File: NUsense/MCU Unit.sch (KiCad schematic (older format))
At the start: 40 parts

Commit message: Correct broken files
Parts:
- removed C? (x13): C, symbol C
- removed R? (x3): R, symbol R
- added C? (x2): 4.7uF, symbol CP
- added C?: 1uF, symbol CP
- added C? (x19): 100nF, symbol C
- added C?: 9pF, symbol C
- added C?: 8pF, symbol C
- added R? (x3): 0, symbol R
- C?: value C -> 9pF
- C?: value C -> 8pF
- C? (x3): value C -> 1uF
- C? (x2): value C -> 0.1uF
- C? (x2): value C -> 2.2uF
- C?: value C -> 100nF
- R? (x2): value R -> 0
- R? (x2): value R -> 10K
- R?: value R -> NC
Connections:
- net labels added: +3.3V, BUZZER_SIG, JTCK_SWCLK, JTD0_SW0, JTDI, JTMS_SWDIO, MCU_RESET, MPU_INT, MPU_SCL, MPU_SDA/SDI, OTG_HS_ULPI_CK, OTG_HS_ULPI_D, OTG_HS_ULPI_DIR, OTG_HS_ULPI_NXT, OTG_HS_ULPI_STP, UART5_RX, UART5_TX, UART7_RX, UART7_TX, UART8_RX, UART8_TX, USART1_RX, USART1_TX, USART2_RX, USART2_TX, USART3_RX, USART3_TX, USART6_RX, USART6_TX
- net labels removed: MCU_NRESET, VDD3o3V
- wire segments 95 -> 145
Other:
- moved on the sheet: C?

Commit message: Main page additions
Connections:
- net labels added: I2C4_INT, I2C4_SCL, I2C4_SDA
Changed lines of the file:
@@
 Text HLabel 12300 7100 0    60   Output ~ 0
 BUZZER_SIG
+Text HLabel 12300 3600 0    60   BiDi ~ 0
+I2C4_SDA
+Text HLabel 12300 3500 0    60   BiDi ~ 0
+I2C4_SCL
+Text HLabel 12300 3400 0    60   BiDi ~ 0
+I2C4_INT
 $EndSCHEMATC

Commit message: Footprints
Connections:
- net labels added: VS_ALERT
- net labels removed: I2C4_INT
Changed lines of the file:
@@
 I2C4_SCL
 Text HLabel 12300 3400 0    60   BiDi ~ 0
-I2C4_INT
+VS_ALERT
 $EndSCHEMATC

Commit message: Adds annotations and footprints
Changes crystal selection
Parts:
- removed C?: 9pF, symbol C
- removed R? (x4): 0, symbol R
- removed Y?: STL9020C-32.768K, symbol STL9020C-32.768K
- removed Y?: SP8150E7-25.000M, symbol SP8150E7-25.000M
- added C310: 10pF, Capacitors_SMD:C_0805_HandSoldering, symbol C
- added X1: 24MHz, Footprints:XTAL-OSC, symbol Crystal_GND24
- added X2: ST3215SB32768H5, Footprints:XTAL, symbol Crystal
- C301, C302, C303, C304, C305, C306, C307, C308, C311, C312, C313, C314, C315, C316, C317, C318, C319, C320, C321, C322, C323, C324, C325, C326, C327, C328, C329, C330, C331, C332, C333, C334: renamed from C?; footprint (none) -> Capacitors_SMD:C_0805_HandSoldering
- C309: renamed from C?; value 9pF -> 10pF; footprint (none) -> Capacitors_SMD:C_0805_HandSoldering
- R305, R306, R307, R308: renamed from R?; footprint (none) -> Resistors_SMD:R_0805_HandSoldering
- U301: renamed from U?; footprint (none) -> Footprints:LQFP144
- gave numbers to parts that had none: 4
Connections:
- net labels added: OSC32_IN, OSC32_OUT, OSC_IN, OSC_OUT, UART5_EN, USART1_EN, USART2_EN, USART3_EN, USART6_EN
- net labels removed: UART7_RX, UART7_TX, UART8_RX, UART8_TX
- wire segments 145 -> 141
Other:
- moved on the sheet: C309, C311, C312

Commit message: More Changes
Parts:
- renumbered C311 to C309, C309 to C310, C313 to C311, C314 to C312, C315 to C313, C316 to C314, C317 to C315, C318 to C316, C312 to C317, C319 to C318, C320 to C319, C310 to C320, R305 to R301, R306 to R302, R307 to R303, R308 to R304, X1 to X301, X2 to X302
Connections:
- net DXL_PWR_EN: now reaches U301.55 (PF15)

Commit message: Buttons/LEDs
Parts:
- added H?: LED_HEADER, symbol LED_HEADER
- added H?: BUT_HEADER, symbol BUT_HEADER
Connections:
- net +3V3: now also H?.3
- net GND: now also H?.1
- new net LED2: H?.7
- new net LED3: H?.6
- new net LED4: H?.5
- new net LED5_B: H?.2
- new net LED5_G: H?.3
- new net LED5_R: H?.4
- new net LED6_B: H?.7
- new net LED6_G: H?.8
- new net LED6_R: H?.1
- new net LED_RX: H?.8
- new net LED_TX: H?.9
- new net RESET: H?.6
- new net SW_MODE: H?.5
- new net SW_START: H?.4
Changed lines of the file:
@@
 Text HLabel 12300 7200 0    60   Output ~ 0
 DXL_PWR_EN
+$Comp
+L LED_HEADER H?
+U 1 1 5A74166C
+P 14650 9700
+F 0 "H?" H 14750 10850 60  0000 C CNN
+F 1 "LED_HEADER" H 14750 9650 60  0000 C CNN
+F 2 "" H 14650 9700 60  0001 C CNN
+F 3 "" H 14650 9700 60  0001 C CNN
+	1    14650 9700
+	1    0    0    -1
+$EndComp
+Wire Wire Line
+	14450 7450 14350 7450
+Wire Wire Line
+	14350 7450 14350 7150
+Wire Wire Line
+	14350 7150 15050 7150
+Wire Wire Line
+	15050 7150 15050 7350
+Wire Wire Line
+	14450 7550 14100 7550
+Wire Wire Line
+	13850 7650 14450 7650
+Wire Wire Line
+	14450 7750 14100 7750
+Wire Wire Line
+	14450 7850 14100 7850
+Wire Wire Line
+	14450 7950 14100 7950
+Wire Wire Line
+	14450 8050 14100 8050
+Wire Wire Line
+	14450 8150 14100 8150
+Text Label 14100 8150 0    60   ~ 0
+LED6_G
+Text Label 14100 8050 0    60   ~ 0
+LED6_B
+Text Label 14100 7950 0    60   ~ 0
+RESET
+Text Label 14100 7850 0    60   ~ 0
+SW_MODE
+Text Label 14100 7750 0    60   ~ 0
+SW_START
+$Comp
+L +3.3V #PWR?
+U 1 1 5A742C85
+P 13850 7600
+F 0 "#PWR?" H 13850 7450 50  0001 C CNN
+F 1 "+3.3V" H 13850 7740 50  0000 C CNN
+F 2 "" H 13850 7600 50  0001 C CNN
+F 3 "" H 13850 7600 50  0001 C CNN
+	1    13850 7600
+	1    0    0    -1
+$EndComp
+Wire Wire Line
+	13850 7600 13850 7650
+$Comp
+L BUT_HEADER H?
+U 1 1 5A743338
+P 14650 8450
+F 0 "H?" H 14750 9600 60  0000 C CNN
+F 1 "BUT_HEADER" H 14750 8600 60  0000 C CNN
+F 2 "" H 14650 8450 60  0001 C CNN
+F 3 "" H 14650 8450 60  0001 C CNN
+	1    14650 8450
+	1    0    0    -1
+$EndComp
+$Comp
+L GND #PWR?
+U 1 1 5A743470
+P 15050 7350
+F 0 "#PWR?" H 15050 7100 50  0001 C CNN
+F 1 "GND" H 15050 7200 50  0000 C CNN
+F 2 "" H 15050 7350 50  0001 C CNN
+F 3 "" H 15050 7350 50  0001 C CNN
+	1    15050 7350
+	1    0    0    -1
+$EndComp
+Wire Wire Line
+	14450 8700 14100 8700
+Wire Wire Line
+	14450 8800 14100 8800
+Wire Wire Line
+	14450 8900 14100 8900
+Wire Wire Line
+	14450 9000 14100 9000
+Wire Wire Line
+	14450 9100 14100 9100
+Wire Wire Line
+	14450 9200 14100 9200
+Wire Wire Line
+	14450 9300 14100 9300
+Wire Wire Line
+	14450 9400 14100 9400
+Wire Wire Line
+	14450 9500 14100 9500
+Text Label 14100 8700 0    60   ~ 0
+LED6_R
+Text Label 14100 8800 0    60   ~ 0
+LED5_B
+Text Label 14100 8900 0    60   ~ 0
+LED5_G
+Text Label 14100 9000 0    60   ~ 0
+LED5_R
+Text Label 14100 9100 0    60   ~ 0
+LED4
+Text Label 14100 9200 0    60   ~ 0
+LED3
+Text Label 14100 9300 0    60   ~ 0
+LED2
+Text Label 14100 9400 0    60   ~ 0
+LED_RX
+Text Label 14100 9500 0    60   ~ 0
+LED_TX
 $EndSCHEMATC

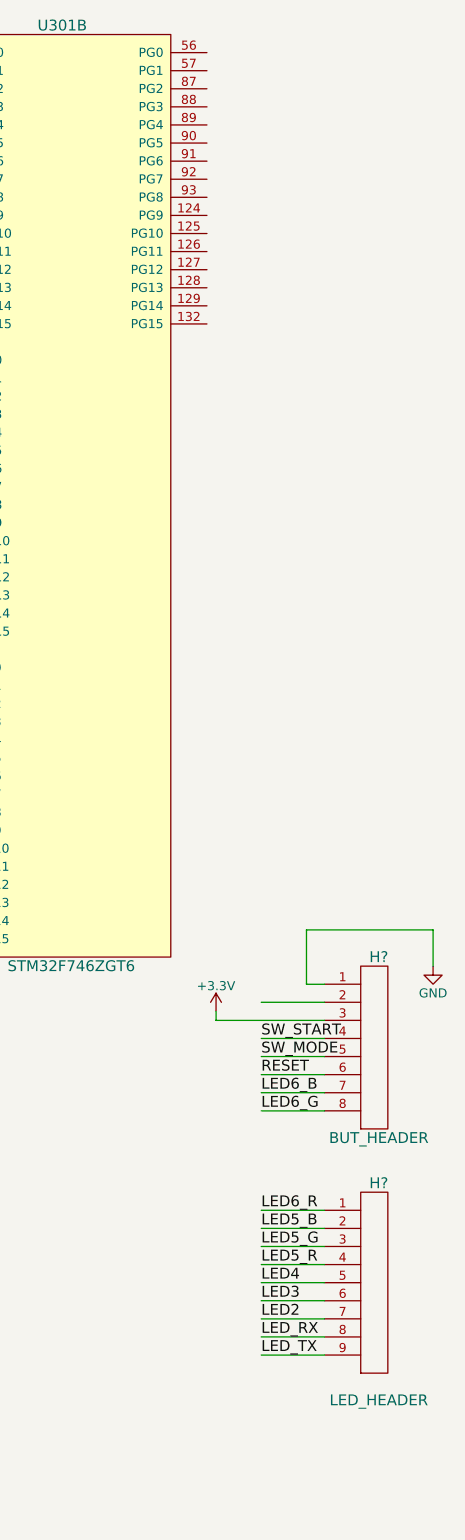
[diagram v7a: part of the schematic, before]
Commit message: Add LED and Button
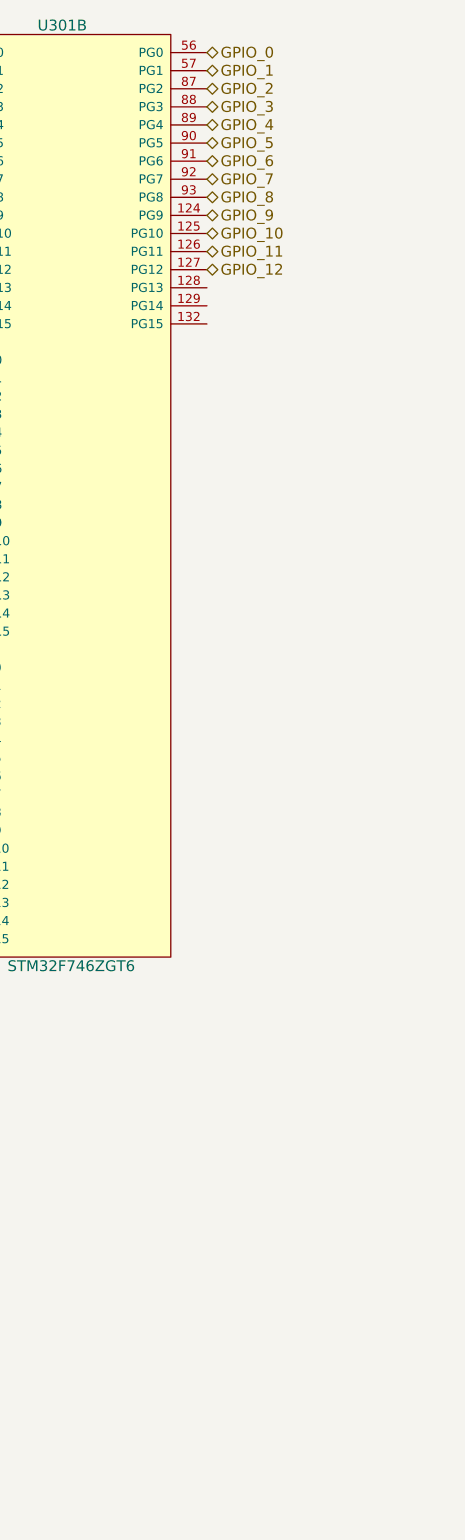
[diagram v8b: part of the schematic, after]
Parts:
- removed H?: LED_HEADER, symbol LED_HEADER
- removed H?: BUT_HEADER, symbol BUT_HEADER
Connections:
- net GPIO_9: now reaches U301.124 (PG9)
- net GPIO_10: now reaches U301.125 (PG10)
- net GPIO_11: now reaches U301.126 (PG11)
- net GPIO_12: now reaches U301.127 (PG12)
- net GPIO_0: now reaches U301.56 (PG0)
- net GPIO_1: now reaches U301.57 (PG1)
- net GPIO_2: now reaches U301.87 (PG2)
- net GPIO_3: now reaches U301.88 (PG3)
- net GPIO_4: now reaches U301.89 (PG4)
- net GPIO_5: now reaches U301.90 (PG5)
- net GPIO_6: now reaches U301.91 (PG6)
- net GPIO_7: now reaches U301.92 (PG7)
- net GPIO_8: now reaches U301.93 (PG8)
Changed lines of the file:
@@
 $EndComp
 $Comp
-L GND #PWR09
+L GND #PWR14
 U 1 1 5A6BFE16
 P 4000 6200
-F 0 "#PWR09" H 4000 5950 50  0001 C CNN
+F 0 "#PWR14" H 4000 5950 50  0001 C CNN
 F 1 "GND" H 4000 6050 50  0000 C CNN
 F 2 "" H 4000 6200 50  0001 C CNN
@@
 $EndComp
 $Comp
-L GND #PWR010
+L GND #PWR11
 U 1 1 5A6BFE38
 P 3200 6950
-F 0 "#PWR010" H 3200 6700 50  0001 C CNN
+F 0 "#PWR11" H 3200 6700 50  0001 C CNN
 F 1 "GND" H 3200 6800 50  0000 C CNN
 F 2 "" H 3200 6950 50  0001 C CNN
@@
 $EndComp
 $Comp
-L GND #PWR011
+L GND #PWR13
 U 1 1 5A6BFE45
 P 3800 7150
-F 0 "#PWR011" H 3800 6900 50  0001 C CNN
+F 0 "#PWR13" H 3800 6900 50  0001 C CNN
 F 1 "GND" H 3800 7000 50  0000 C CNN
 F 2 "" H 3800 7150 50  0001 C CNN
@@
 $EndComp
 $Comp
-L GND #PWR012
+L GND #PWR9
 U 1 1 5A6BFE4B
 P 2650 7150
-F 0 "#PWR012" H 2650 6900 50  0001 C CNN
+F 0 "#PWR9" H 2650 6900 50  0001 C CNN
 F 1 "GND" H 2650 7000 50  0000 C CNN
 F 2 "" H 2650 7150 50  0001 C CNN
@@
 $EndComp
 $Comp
-L GND #PWR013
+L GND #PWR16
 U 1 1 5A6BFE84
 P 4950 8100
-F 0 "#PWR013" H 4950 7850 50  0001 C CNN
+F 0 "#PWR16" H 4950 7850 50  0001 C CNN
 F 1 "GND" H 4950 7950 50  0000 C CNN
 F 2 "" H 4950 8100 50  0001 C CNN
@@
 $EndComp
 $Comp
-L GND #PWR014
+L GND #PWR21
 U 1 1 5A6BFE8A
 P 6700 7300
-F 0 "#PWR014" H 6700 7050 50  0001 C CNN
+F 0 "#PWR21" H 6700 7050 50  0001 C CNN
 F 1 "GND" H 6700 7150 50  0000 C CNN
 F 2 "" H 6700 7300 50  0001 C CNN
@@
 $EndComp
 $Comp
-L GND #PWR015
+L GND #PWR26
 U 1 1 5A6BFEA7
 P 8750 9450
-F 0 "#PWR015" H 8750 9200 50  0001 C CNN
+F 0 "#PWR26" H 8750 9200 50  0001 C CNN
 F 1 "GND" H 8750 9300 50  0000 C CNN
 F 2 "" H 8750 9450 50  0001 C CNN
@@
 $EndComp
 $Comp
-L GND #PWR016
+L GND #PWR23
 U 1 1 5A6BFEDA
 P 8050 10650
-F 0 "#PWR016" H 8050 10400 50  0001 C CNN
+F 0 "#PWR23" H 8050 10400 50  0001 C CNN
 F 1 "GND" H 8050 10500 50  0000 C CNN
 F 2 "" H 8050 10650 50  0001 C CNN
@@
 $EndComp
 $Comp
-L GND #PWR017
+L GND #PWR25
 U 1 1 5A6BFEE0
 P 8400 10650
-F 0 "#PWR017" H 8400 10400 50  0001 C CNN
+F 0 "#PWR25" H 8400 10400 50  0001 C CNN
 F 1 "GND" H 8400 10500 50  0000 C CNN
 F 2 "" H 8400 10650 50  0001 C CNN
@@
 $EndComp
 $Comp
-L GND #PWR018
+L GND #PWR27
 U 1 1 5A6BFEE6
 P 8750 10650
-F 0 "#PWR018" H 8750 10400 50  0001 C CNN
+F 0 "#PWR27" H 8750 10400 50  0001 C CNN
 F 1 "GND" H 8750 10500 50  0000 C CNN
 F 2 "" H 8750 10650 50  0001 C CNN
@@
 $EndComp
 $Comp
-L GND #PWR019
+L GND #PWR28
 U 1 1 5A6BFEEC
 P 9050 10650
-F 0 "#PWR019" H 9050 10400 50  0001 C CNN
+F 0 "#PWR28" H 9050 10400 50  0001 C CNN
 F 1 "GND" H 9050 10500 50  0000 C CNN
 F 2 "" H 9050 10650 50  0001 C CNN
@@
 $EndComp
 $Comp
-L GND #PWR020
+L GND #PWR29
 U 1 1 5A6BFEF3
 P 11000 9500
-F 0 "#PWR020" H 11000 9250 50  0001 C CNN
+F 0 "#PWR29" H 11000 9250 50  0001 C CNN
 F 1 "GND" H 11000 9350 50  0000 C CNN
 F 2 "" H 11000 9500 50  0001 C CNN
@@
 $EndComp
 $Comp
-L GND #PWR021
+L GND #PWR30
 U 1 1 5A6BFF00
 P 11000 10500
-F 0 "#PWR021" H 11000 10250 50  0001 C CNN
+F 0 "#PWR30" H 11000 10250 50  0001 C CNN
 F 1 "GND" H 11000 10350 50  0000 C CNN
 F 2 "" H 11000 10500 50  0001 C CNN
@@
 $EndComp
 $Comp
-L GND #PWR022
+L GND #PWR31
 U 1 1 5A6BFF06
 P 11300 10500
-F 0 "#PWR022" H 11300 10250 50  0001 C CNN
+F 0 "#PWR31" H 11300 10250 50  0001 C CNN
 F 1 "GND" H 11300 10350 50  0000 C CNN
 F 2 "" H 11300 10500 50  0001 C CNN
@@
 $EndComp
 $Comp
-L GND #PWR023
+L GND #PWR15
 U 1 1 5A6BFF68
 P 4550 10350
-F 0 "#PWR023" H 4550 10100 50  0001 C CNN
+F 0 "#PWR15" H 4550 10100 50  0001 C CNN
 F 1 "GND" H 4550 10200 50  0000 C CNN
 F 2 "" H 4550 10350 50  0001 C CNN
@@
 OTG_HS_ULPI_D
 $Comp
-L +3.3V #PWR024
+L +3.3V #PWR20
 U 1 1 5A6FCDF0
 P 6700 7000
-F 0 "#PWR024" H 6700 6850 50  0001 C CNN
+F 0 "#PWR20" H 6700 6850 50  0001 C CNN
 F 1 "+3.3V" H 6700 7140 50  0000 C CNN
 F 2 "" H 6700 7000 50  0001 C CNN
@@
 $EndComp
 $Comp
-L +3.3V #PWR025
+L +3.3V #PWR18
 U 1 1 5A6FCE7A
 P 5800 7500
-F 0 "#PWR025" H 5800 7350 50  0001 C CNN
+F 0 "#PWR18" H 5800 7350 50  0001 C CNN
 F 1 "+3.3V" H 5800 7640 50  0000 C CNN
 F 2 "" H 5800 7500 50  0001 C CNN
@@
 $EndComp
 $Comp
-L +3.3V #PWR026
+L +3.3V #PWR24
 U 1 1 5A6FD2DC
 P 8250 8400
-F 0 "#PWR026" H 8250 8250 50  0001 C CNN
+F 0 "#PWR24" H 8250 8250 50  0001 C CNN
 F 1 "+3.3V" H 8250 8540 50  0000 C CNN
 F 2 "" H 8250 8400 50  0001 C CNN
@@
 VDD3o3V_MCU
 $Comp
-L GND #PWR027
+L GND #PWR17
 U 1 1 5A701246
 P 5500 9800
-F 0 "#PWR027" H 5500 9550 50  0001 C CNN
+F 0 "#PWR17" H 5500 9550 50  0001 C CNN
 F 1 "GND" H 5500 9650 50  0000 C CNN
 F 2 "" H 5500 9800 50  0001 C CNN
@@
 VDD_REF+
 $Comp
-L GND #PWR028
+L GND #PWR19
 U 1 1 5A7014A6
 P 6300 10750
-F 0 "#PWR028" H 6300 10500 50  0001 C CNN
+F 0 "#PWR19" H 6300 10500 50  0001 C CNN
 F 1 "GND" H 6300 10600 50  0000 C CNN
 F 2 "" H 6300 10750 50  0001 C CNN
@@
 	8400 9650 8400 10300
 $Comp
-L +3.3V #PWR029
+L +3.3V #PWR22
 U 1 1 5A6FD08D
 P 6900 9900
-F 0 "#PWR029" H 6900 9750 50  0001 C CNN
+F 0 "#PWR22" H 6900 9750 50  0001 C CNN
 F 1 "+3.3V" H 6900 10040 50  0000 C CNN
 F 2 "" H 6900 9900 50  0001 C CNN
@@
 $EndComp
 $Comp
-L GND #PWR030
+L GND #PWR10
 U 1 1 5A6BFE10
 P 2700 6200
-F 0 "#PWR030" H 2700 5950 50  0001 C CNN
+F 0 "#PWR10" H 2700 5950 50  0001 C CNN
 F 1 "GND" H 2700 6050 50  0000 C CNN
 F 2 "" H 2700 6200 50  0001 C CNN
@@
 	5150 5800 4600 5800
 $Comp
-L GND #PWR031
+L GND #PWR12
 U 1 1 5A7647F9
 P 3400 6450
-F 0 "#PWR031" H 3400 6200 50  0001 C CNN
+F 0 "#PWR12" H 3400 6200 50  0001 C CNN
 F 1 "GND" H 3400 6300 50  0000 C CNN
 F 2 "" H 3400 6450 50  0001 C CNN
@@
 Text HLabel 12300 7200 0    60   Output ~ 0
 DXL_PWR_EN
-$Comp
-L LED_HEADER H?
-U 1 1 5A74166C
-P 14650 9700
-F 0 "H?" H 14750 10850 60  0000 C CNN
-F 1 "LED_HEADER" H 14750 9650 60  0000 C CNN
-F 2 "" H 14650 9700 60  0001 C CNN
-F 3 "" H 14650 9700 60  0001 C CNN
-	1    14650 9700
-	1    0    0    -1
-$EndComp
-Wire Wire Line
-	14450 7450 14350 7450
-Wire Wire Line
-	14350 7450 14350 7150
-Wire Wire Line
-	14350 7150 15050 7150
-Wire Wire Line
-	15050 7150 15050 7350
-Wire Wire Line
-	14450 7550 14100 7550
-Wire Wire Line
-	13850 7650 14450 7650
-Wire Wire Line
-	14450 7750 14100 7750
-Wire Wire Line
-	14450 7850 14100 7850
-Wire Wire Line
-	14450 7950 14100 7950
-Wire Wire Line
-	14450 8050 14100 8050
-Wire Wire Line
-	14450 8150 14100 8150
-Text Label 14100 8150 0    60   ~ 0
-LED6_G
-Text Label 14100 8050 0    60   ~ 0
-LED6_B
-Text Label 14100 7950 0    60   ~ 0
-RESET
-Text Label 14100 7850 0    60   ~ 0
-SW_MODE
-Text Label 14100 7750 0    60   ~ 0
-SW_START
-$Comp
-L +3.3V #PWR032
-U 1 1 5A742C85
-P 13850 7600
-F 0 "#PWR032" H 13850 7450 50  0001 C CNN
-F 1 "+3.3V" H 13850 7740 50  0000 C CNN
-F 2 "" H 13850 7600 50  0001 C CNN
-F 3 "" H 13850 7600 50  0001 C CNN
-	1    13850 7600
-	1    0    0    -1
-$EndComp
-Wire Wire Line
-	13850 7600 13850 7650
-$Comp
-L BUT_HEADER H?
-U 1 1 5A743338
-P 14650 8450
-F 0 "H?" H 14750 9600 60  0000 C CNN
-F 1 "BUT_HEADER" H 14750 8600 60  0000 C CNN
-F 2 "" H 14650 8450 60  0001 C CNN
-F 3 "" H 14650 8450 60  0001 C CNN
-	1    14650 8450
-	1    0    0    -1
-$EndComp
-$Comp
-L GND #PWR033
-U 1 1 5A743470
-P 15050 7350
-F 0 "#PWR033" H 15050 7100 50  0001 C CNN
-F 1 "GND" H 15050 7200 50  0000 C CNN
-F 2 "" H 15050 7350 50  0001 C CNN
-F 3 "" H 15050 7350 50  0001 C CNN
-	1    15050 7350
-	1    0    0    -1
-$EndComp
-Wire Wire Line
-	14450 8700 14100 8700
-Wire Wire Line
-	14450 8800 14100 8800
-Wire Wire Line
-	14450 8900 14100 8900
-Wire Wire Line
-	14450 9000 14100 9000
-Wire Wire Line
-	14450 9100 14100 9100
-Wire Wire Line
-	14450 9200 14100 9200
-Wire Wire Line
-	14450 9300 14100 9300
-Wire Wire Line
-	14450 9400 14100 9400
-Wire Wire Line
-	14450 9500 14100 9500
-Text Label 14100 8700 0    60   ~ 0
-LED6_R
-Text Label 14100 8800 0    60   ~ 0
-LED5_B
-Text Label 14100 8900 0    60   ~ 0
-LED5_G
-Text Label 14100 9000 0    60   ~ 0
-LED5_R
-Text Label 14100 9100 0    60   ~ 0
-LED4
-Text Label 14100 9200 0    60   ~ 0
-LED3
-Text Label 14100 9300 0    60   ~ 0
-LED2
-Text Label 14100 9400 0    60   ~ 0
-LED_RX
-Text Label 14100 9500 0    60   ~ 0
-LED_TX
+Text HLabel 13800 2300 2    60   BiDi ~ 0
+GPIO_0
+Text HLabel 13800 2400 2    60   BiDi ~ 0
+GPIO_1
+Text HLabel 13800 2500 2    60   BiDi ~ 0
+GPIO_2
+Text HLabel 13800 2600 2    60   BiDi ~ 0
+GPIO_3
+Text HLabel 13800 2700 2    60   BiDi ~ 0
+GPIO_4
+Text HLabel 13800 2800 2    60   BiDi ~ 0
+GPIO_5
+Text HLabel 13800 2900 2    60   BiDi ~ 0
+GPIO_6
+Text HLabel 13800 3000 2    60   BiDi ~ 0
+GPIO_7
+Text HLabel 13800 3100 2    60   BiDi ~ 0
+GPIO_8
+Text HLabel 13800 3200 2    60   BiDi ~ 0
+GPIO_9
+Text HLabel 13800 3300 2    60   BiDi ~ 0
+GPIO_10
+Text HLabel 13800 3400 2    60   BiDi ~ 0
+GPIO_11
+Text HLabel 13800 3500 2    60   BiDi ~ 0
+GPIO_12
 $EndSCHEMATC
